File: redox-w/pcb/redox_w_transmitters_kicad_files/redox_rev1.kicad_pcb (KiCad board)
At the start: 2 copper layers, 162.2 x 126.5 mm, 104 parts, among them K0 KEYSW, K1 KEYSW, K10 KEYSW, K11 KEYSW, K12 KEYSW, K13 KEYSW, K14 KEYSW, K15 KEYSW, K16 KEYSW, K2 KEYSW, K20 KEYSW, K21 KEYSW, K22 KEYSW, K23 KEYSW, K24 KEYSW, K25 KEYSW, K26 KEYSW, K3 KEYSW, K30 KEYSW, K31 KEYSW, K32 KEYSW, K33 KEYSW, K34 KEYSW, K35 KEYSW, K36 KEYSW, K4 KEYSW, K40 KEYSW, K41 KEYSW, K42 KEYSW, K43 KEYSW, K44 KEYSW, K45 KEYSW, K46 KEYSW, K5 KEYSW, K6 KEYSW

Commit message: wip
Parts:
- removed C_LEFT1, C_RIGHT1: 1 μF, Capacitor_SMD:C_0805_2012Metric_Pad1.15x1.40mm_HandSolder
- removed JP_LEFT1, JP_RIGHT2: SolderJumper_2_Bridged, Jumper:SolderJumper-2_P1.3mm_Bridged2Bar_Pad1.0x1.5mm
- removed JP_LEFT2, JP_RIGHT1: SolderJumper_2_Open, Jumper:SolderJumper-2_P1.3mm_Bridged2Bar_Pad1.0x1.5mm
- added C_1: 1 μF, Capacitor_SMD:C_0805_2012Metric_Pad1.15x1.40mm_HandSolder, F.Cu at (139.3, 54.3)
- added R3: 4.7k, Resistor_SMD:R_0805_2012Metric_Pad1.15x1.40mm_HandSolder, F.Cu at (140.5, 50.7)
- moved SW_LEFT1 8.97 mm to (109.4, 31.4)
- moved U_RIGHT2 1.04 mm to (133.6, 52.0)
- moved Q_LEFT1 1.04 mm to (129.0, 51.9)
- moved Q_RIGHT1 1.04 mm to (129.0, 51.9)
- moved U_LEFT2 1.04 mm to (133.6, 51.9)
- renumbered U_RIGHT2 to U_LEFT3, U_RIGHT3 to U_RIGHT2
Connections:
- TRRS1 pad 1: VCC1 -> VCC
- U_LEFT1 pad 16: Net-(U_LEFT1-Pad16) -> ON_BATT
- U_LEFT2 pad 4: Net-(U_LEFT2-Pad4) -> ON_BATT
- U_RIGHT1 pad 21: Net-(U_RIGHT1-Pad21) -> ON_BATT
- U_RIGHT2 pad 4: Net-(U_RIGHT3-Pad4) -> ON_BATT
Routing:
- net ON_BATT: track 0.00 -> 101.9 mm, vias 0 -> 3
- net SCL2: track 0.00 -> 97.1 mm, vias 0 -> 1
- net SDA2: track 0.00 -> 93.2 mm, vias 0 -> 1
- net VCC1: track 51.0 -> 0.00 mm, vias 1 -> 0
- net (no net): track 19.9 -> 0.00 mm
- net VCC: track 192.0 -> 200.9 mm
- net Net-(BT_RIGHT1-Pad1): track 53.4 -> 52.4 mm

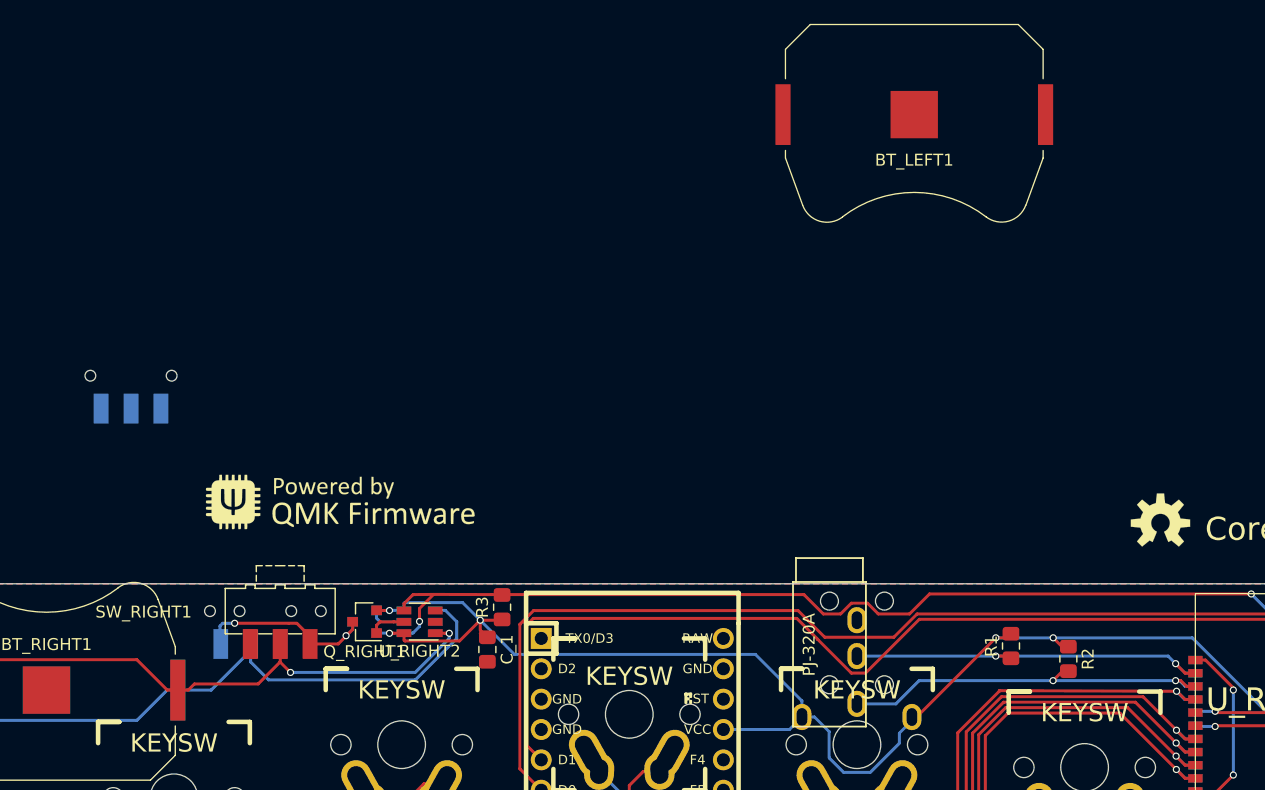
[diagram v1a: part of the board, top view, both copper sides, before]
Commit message: Roughly Finished PCB - Changed To Not Mirror Power Circuit
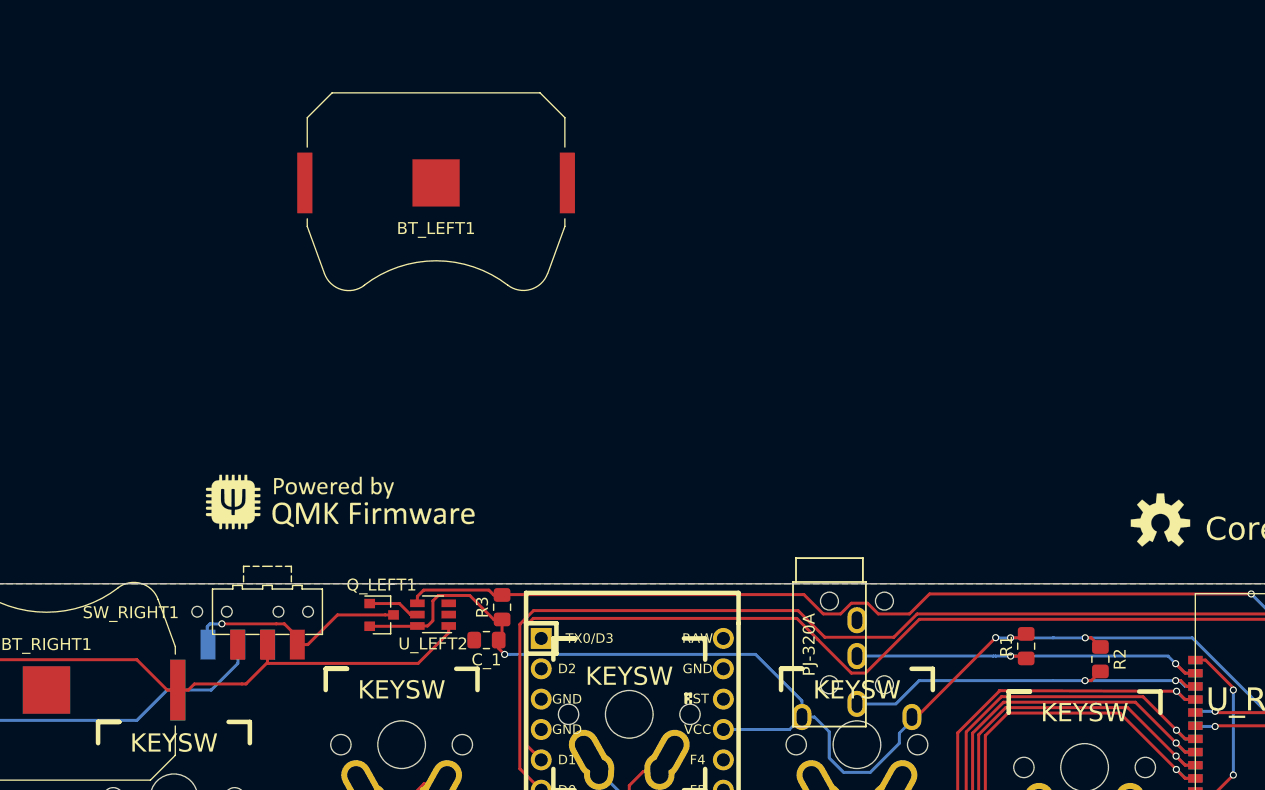
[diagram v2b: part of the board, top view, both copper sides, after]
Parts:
- removed Q_RIGHT1: DMG2301L, Package_TO_SOT_SMD:SOT-23
- removed the SW_LEFT1 at (109.4, 31.4)
- removed the SW_LEFT1 at (119.4, 51.1)
- removed U_RIGHT2: LTC4412xS6, Package_TO_SOT_SMD:TSOT-23-6
- added SW_LEFT1: SW_SPDT, redox_w_footprints:SW_SPDT_CK-JS102011SAQN, B.Cu at (118.4, 51.1)
- Q_LEFT1, U_LEFT2: moved to F.Cu
- moved BT_LEFT1 40.4 mm to (135.0, 15.2)
- moved R2 2.68 mm to (190.6, 55.1)
- moved Q_LEFT1 1.53 mm to (130.4, 51.4), turned to 0 degrees
- moved U_LEFT2 1.28 mm to (134.7, 51.3)
- moved R1 1.27 mm to (184.3, 54.0)
- moved SW_RIGHT1 1.07 mm to (120.9, 51.1)
- moved C_1 0.79 mm to (139.2, 53.5), turned to 180 degrees
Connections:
- BT_RIGHT1 pad 1: Net-(BT_RIGHT1-Pad1) -> Net-(BT_LEFT1-Pad1)
- SW_RIGHT1 pad 1: Net-(Q_RIGHT1-Pad3) -> Net-(Q_LEFT1-Pad3)
- SW_RIGHT1 pad 2: Net-(BT_RIGHT1-Pad1) -> Net-(BT_LEFT1-Pad1)
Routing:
- net Net-(BT_RIGHT1-Pad1): track 52.4 -> 0.00 mm, vias 2 -> 0
- net Net-(BT_LEFT1-Pad1): track 56.5 -> 82.5 mm
- net Net-(Q_LEFT1-Pad3): track 1.39 -> 19.3 mm, vias 0 -> 1
- net Net-(Q_RIGHT1-Pad3): track 14.9 -> 0.00 mm, vias 2 -> 0
- net VCC: track 200.9 -> 190.9 mm, vias 7 -> 6
- net ON_BATT: track 101.9 -> 95.6 mm, vias 3 -> 2
- net Net-(Q_RIGHT1-Pad1): track 3.07 -> 0.00 mm
- net Net-(Q_LEFT1-Pad1): track 3.06 -> 4.38 mm

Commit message: OK, NOW we're roughly done
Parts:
- removed the BT_LEFT1 at (102.4, 57.7)
- BT_LEFT1: moved to B.Cu
- moved BT_LEFT1 53.5 mm to (102.3, 57.7)
- moved R3 1.79 mm to (138.7, 50.9), turned to 0 degrees
- moved R1 0.80 mm to (183.5, 54.1)
- moved C_1 0.75 mm to (138.7, 52.9)
- moved Q_LEFT1 0.37 mm to (130.3, 51.7)
- moved U_LEFT2 0.37 mm to (134.6, 51.7)
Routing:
- net GND: track 15.2 -> 18.4 mm
- net ON_BATT: track 95.6 -> 98.4 mm
- net VCC: track 190.9 -> 190.5 mm, vias 6 -> 5
- net PROG_SWCLK: vias 1 -> 2
- net PROG_SWDIO: vias 1 -> 2

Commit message: PCB Roughly Finished - All Labels In Place
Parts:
- removed the ? at (195.6, 43.7) (x2)
- removed the G*** at (127.3, 42.2)
- removed the G*** at (127.0, 41.9)
- added ?: , Sparkfun-Aesthetics:OSHW-LOGO-M, B.Cu at (178.1, 51.8)
- added ?: , Sparkfun-Aesthetics:OSHW-LOGO-M, F.Cu at (178.1, 51.8)
- added G***: LOGO, myparts:qmk-badge, B.Cu at (211.6, 142.0)
- added G***: LOGO, myparts:qmk-badge, F.Cu at (211.6, 142.2)
- added R4: 4.7k, Resistor_SMD:R_0805_2012Metric_Pad1.15x1.40mm_HandSolder, B.Cu at (151.1, 53.6)
- added R5: 4.7k, Resistor_SMD:R_0805_2012Metric_Pad1.15x1.40mm_HandSolder, B.Cu at (153.2, 53.6)
- moved G*** 56.7 mm to (122.9, 96.5)
- moved G*** 56.7 mm to (122.4, 96.5)
- renumbered C_1 to C2, Q_LEFT1 to Q1, U_LEFT2 to U1
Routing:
- net SCL2: track 97.1 -> 98.7 mm, vias 1 -> 2
- net SDA2: track 93.2 -> 94.7 mm, vias 1 -> 2
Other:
- board text added: "Modified by Gareth Ellis (github.com/garethellis0)"

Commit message: Tweaking After Checking JLcPCB Submission
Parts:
- renumbered U_LEFT3 to U_LEFT2
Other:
- board text added: "modified by Gareth Ellis (github.com/garethellis0)"
- board text removed: "Modified by Gareth Ellis (github.com/garethellis0)"

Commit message: More Logo Tweaking
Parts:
- moved G*** 21.9 mm to (101.9, 102.8)
- moved G*** 21.4 mm to (101.9, 102.8)
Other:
- board text added: "rev 1.0W&W"
- board text removed: "rev 1.0W"
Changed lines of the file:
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@@
   )
   (module myparts:redox-logo (layer F.Cu)
-    (at 122.428 96.52 90)
+    (at 101.9302 102.7684 90)
     (fp_text reference G*** (at 0 0 90) (layer F.SilkS) hide
       (effects (font (size 1.524 1.524) (thickness 0.3)))
@@
   )
   (module myparts:redox-logo (layer B.Cu)
-    (at 122.936 96.52 270)
+    (at 101.9302 102.8192 270)
     (fp_text reference G*** (at 0 0 270) (layer B.SilkS) hide
       (effects (font (size 1.524 1.524) (thickness 0.3)) (justify mirror))
@@
     )
   )
-  (gr_text "modified by Gareth Ellis (github.com/garethellis0)" (at 101.6 97.536 90) (layer B.SilkS)
+  (gr_text "modified by Gareth Ellis (github.com/garethellis0)" (at 122.555 91.2876 90) (layer B.SilkS)
     (effects (font (size 1.5 1.5) (thickness 0.3)) (justify mirror))
   )
-  (gr_text "modified by Gareth Ellis (github.com/garethellis0)" (at 101.6 97.536 90) (layer F.SilkS)
+  (gr_text "modified by Gareth Ellis (github.com/garethellis0)" (at 122.5042 90.8304 90) (layer F.SilkS)
     (effects (font (size 1.5 1.5) (thickness 0.3)))
   )
-  (gr_text "rev 1.0W" (at 105.41 130.81 90) (layer B.SilkS)
+  (gr_text "rev 1.0W&W" (at 105.41 130.81 90) (layer B.SilkS)
     (effects (font (size 1.5 1.5) (thickness 0.3)) (justify mirror))
   )
@@
     (effects (font (size 1 1) (thickness 0.2)) (justify left))
   )
-  (gr_text "rev 1.0W" (at 105.41 74.93 90) (layer F.SilkS)
+  (gr_text "rev 1.0W&W" (at 105.283 74.7014 90) (layer F.SilkS)
     (effects (font (size 1.5 1.5) (thickness 0.3)))
   )

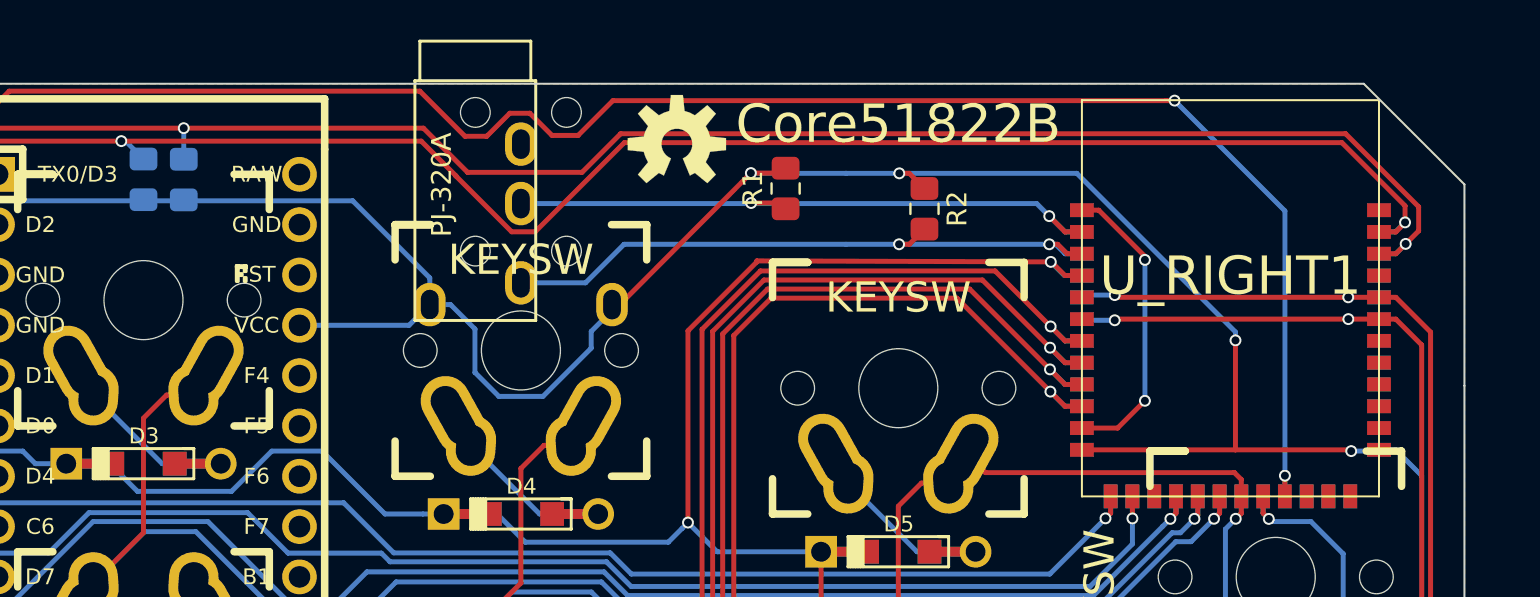
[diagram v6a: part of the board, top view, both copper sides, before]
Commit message: Fixed Bug Where row1 and row2 Were on NC's
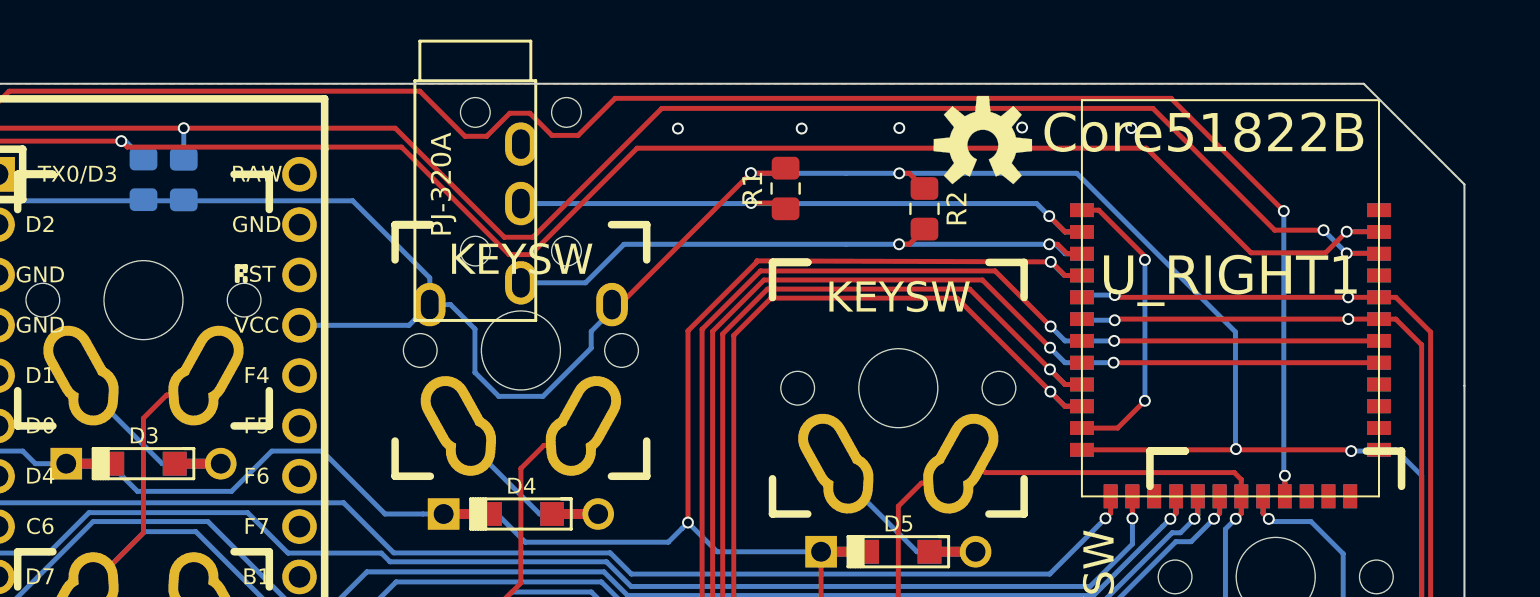
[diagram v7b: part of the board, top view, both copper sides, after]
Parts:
- moved ? 15.4 mm to (193.5, 51.9) (x2)
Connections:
- U_RIGHT1 pad 29: Net-(U_RIGHT1-Pad29) -> row2
- U_RIGHT1 pad 30: Net-(U_RIGHT1-Pad30) -> row1
- U_RIGHT1 pad 7: row1 -> Net-(U_RIGHT1-Pad7)
- U_RIGHT1 pad 8: row2 -> Net-(U_RIGHT1-Pad8)
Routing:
- net row1: track 193.0 -> 206.1 mm, vias 3 -> 4
- net row2: track 221.8 -> 234.9 mm, vias 3 -> 4
- net SDA2: track 94.7 -> 93.3 mm
- net SCL2: track 98.7 -> 97.9 mm, vias 2 -> 3
- net GND: vias 2 -> 7
